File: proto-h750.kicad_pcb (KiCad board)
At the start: 2 copper layers, 63.5 x 73.7 mm, 63 parts, among them J1 Micro_SD_Card, J2 USB_B_Micro, J3 USB_B_Micro, J4 Conn_02x14_Odd_Even, J5 Conn_02x14_Odd_Even, J6 Conn_02x08_Odd_Even, J7 Conn_02x02_Odd_Even, J8 USB_B_Micro, J9 Conn_02x04_Odd_Even, SW1 SW_Push, SW2 SW_Push, SW3 SW_DIP_x01, U1 S25FL132K0XMFI010, U2 STM32H750VBT6, U3 AP1117-33, U4 KSZ8081RNA, Y1 16MHz, Y2 32.768KHz

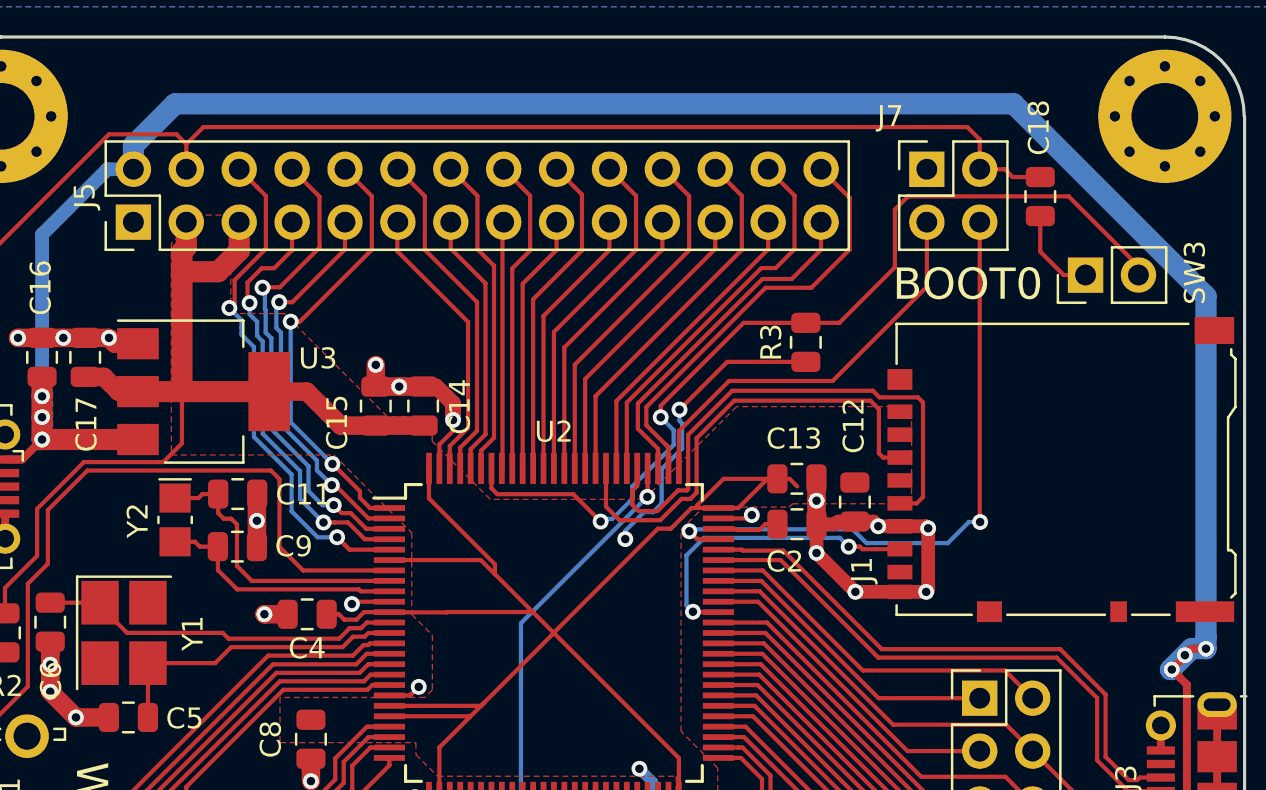
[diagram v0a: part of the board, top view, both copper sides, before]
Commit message: Prepare to BOM (3)
 - Add pull-up on reset
 - Generate Gerbers in protel format-name

Signed-off-by: Martin Ribelotta <martinribelotta@gmail.com>
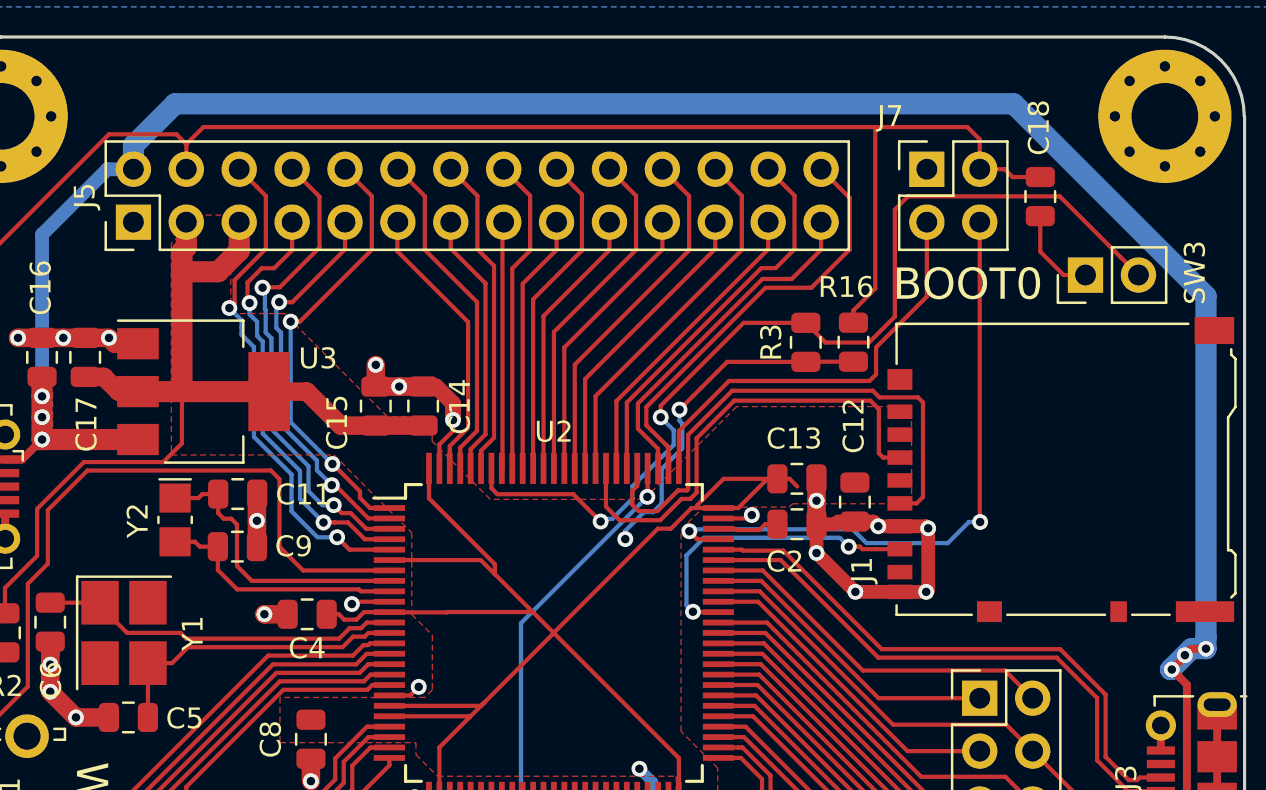
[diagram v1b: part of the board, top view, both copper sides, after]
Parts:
- added R16: 10K, Resistor_SMD:R_0805_2012Metric, F.Cu at (143.8, 56.6)
- C19, C22, C23: value 0.1u -> 100n
- R10, R11, R12, R13, R14, R15, R8, R9: value 22R -> 0R
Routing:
- net /nRESET: track 124.0 -> 133.8 mm
- net VCC: track 218.7 -> 221.0 mm
- net /BOOT: track 44.9 -> 46.8 mm
- net /SWCLK: track 19.7 -> 20.7 mm
